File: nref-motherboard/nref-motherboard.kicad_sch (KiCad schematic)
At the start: 219 parts, among them J1 PWR, J10 1-2199230-6, J10 DISP, J11 BAT1, J12 BAT2, J13 SYSCTL_USB, J16 Conn_01x10_Pin, J17 Conn_01x10_Pin, J17 POWSW, J18 Conn_01x20, J19 SER, J2 Conn_01x12_Pin, J5 SYSCTL, J6 USB_INT1, J8 Conn_01x12_Pin, J9 Conn_01x14_Pin, Q1 NTMFD6H840NL, Q2 NTMFD6H840NL, SW2 RESET, SW4 SW_DIP_x08, U1 reform2-som-connector, U10 BQ25756RRVR, U10 W25Q32JVSS, U11 LM62460, U2 MAX1837EUT33+T, U26 74HC573, U4 Si52111-B5, U5 LM62460, U6 PCF8523T, U7 USB2514B_Bi, U8 RP2040, Y2 12MHz 18pF, Y2 24MHz, Y3 25MHz, Y4 32.768 kHz

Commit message: motherboard: specify all parts, complete BOM
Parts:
- C11, C62: Manufacturer_No CL10B103KB8NNNC -> CL05B104KO5NNNC
- C11, C14, C16, C57, C6, C67, C68, C69, C70, C71: Manufacturer_No GRM188R60J476ME15D -> GRM187R61A226ME15D
- C13, C15, C17, C64, C65, C72, C73, C9: MPN CC0402KRX7R7BB104 -> (none); Manufacturer Yageo -> Samsung; Manufacturer_No (none) -> CL05B104KO5NNNC
- C40, C41, C46, C47: Manufacturer (none) -> Taiyo Yuden; Manufacturer_No (none) -> TMK325ABJ476MM-P
- C42, C43, C44, C45, C48, C49: value 100nF -> 0.1uF; Manufacturer (none) -> Samsung; Manufacturer_No (none) -> CL05B104KO5NNNC
- C50: Manufacturer (none) -> Samsung; Manufacturer_No (none) -> CL05Y474KP5VPJC
- C51: Manufacturer (none) -> Samsung; Manufacturer_No (none) -> CL05A104KA5NNNC
- C52, C53: Manufacturer (none) -> Murata; Manufacturer_No (none) -> GRM155C61E475ME15D
- C54, C59, C61, C7: Manufacturer_No CL10B103KB8NNNC -> CL10A474KB8NNNC
- C56, C60: Manufacturer_No CL10B103KB8NNNC -> CL05A104KA5NNNC
- C7, C74, C76, C8: MPN CC0402FRNPO9BN180 -> (none); Manufacturer_No (none) -> CC0402JRNPO9BN180
- C78: Manufacturer Samsung -> Murata; Manufacturer_No CL05B104KO5NNNC -> GRM155C61E475ME15D
- D10, D11, D4: Manufacturer (none) -> Everlight; Manufacturer_No (none) -> 19-217/R6C-AL1M2VY/3T
- D2, D3: Manufacturer (none) -> Taiwan Semi; Manufacturer_No (none) -> TS4148 RCG
- D8, D9: Manufacturer (none) -> Diodes; Manufacturer_No (none) -> SBR1A20T5-7
- H2, H3, H4, H5, H6, H7, R53, TP1, TP2, TP3, TP4: Manufacturer (none) -> DNP; Manufacturer_No (none) -> DNP; now not fitted
- H5: Manufacturer Wurth -> Würth
- J1: Manufacturer HR(Joint Tech Elec) -> JST; Manufacturer_No A2001WR-S-09PD01 -> SM09B-SRSS-TB
- J10, J19: Manufacturer (none) -> JST; Manufacturer_No (none) -> SM06B-SRSS-TB
- J11, J12: Manufacturer (none) -> JST; Manufacturer_No (none) -> SM07B-SRSS-TB
- J13, J5, J6: Manufacturer_No SM04B-SRSS-TB(LF)(SN) -> SM04B-SRSS-TB
- J16, J17: Manufacturer (none) -> Hirose; Manufacturer_No (none) -> FH12-10S-0.5SH(55)
- J17: Manufacturer_No SM02B-SRSS-TB(LF)(SN) -> SM02B-SRSS-TB
- J2, J8: Manufacturer (none) -> Hirose; Manufacturer_No (none) -> FH12-12S-0.5SH(55)
- J9: Manufacturer (none) -> Hirose; Manufacturer_No (none) -> FH12-14S-0.5SH(55)
- L3: LCSC C511026 -> (none); Manufacturer Vishay -> Bourns; Manufacturer_No IHLP4040DZER150M11 -> SRP6030CA-2R2M
- L3: LCSC C511026 -> (none); Manufacturer Vishay -> Pulse; Manufacturer_No IHLP4040DZER150M11 -> PM2205.332NLT
- L5: Manufacturer (none) -> Bourns; Manufacturer_No (none) -> SRP6060FA-100M
- Q1, Q2: Manufacturer (none) -> onsemi; Manufacturer_No (none) -> NVMFD6H840NLWFT1G
- R10: Manufacturer (none) -> Yageo; Manufacturer_No (none) -> RC0402FR-071ML
- R11, R46, R9: Manufacturer Panasonic -> Vishay; Manufacturer_No ERJ2GE0R00X -> CRCW04020000Z0EDC
- R11, R52, R61, R8, R9: Manufacturer (none) -> Yageo; Manufacturer_No (none) -> RC0402FR-0710RL
- R12, R7: Manufacturer (none) -> Ohmite; Manufacturer_No (none) -> LVT12R0050FER
- R15, R26: Manufacturer_No RC0402FR-0710KL -> RC0402FR-07100KL
- R15, R35, R4, R5: MPN CRCW040250K0FKED -> (none); Manufacturer Vishay / Dale -> Yageo; Manufacturer_No (none) -> RC0402FR-0747KL
- R16, R19: Manufacturer_No RC0402FR-07100KL -> RC0402FR-071KL
- R16: Manufacturer_No RC0402FR-073K16L -> RC0402FR-0724K9L
- R18, R31: Manufacturer_No RC0402FR-0710KL -> RC0402FR-074K99L
- R22: MPN RC0402FR-1312KL -> (none); Manufacturer_No (none) -> RC0402FR-0712KL
- R30: Manufacturer_No RC0402FR-073K16L -> RC0402FR-0743K2L
- R34, R69: MPN RC0402FR-071ML -> (none); Manufacturer_No (none) -> RC0402FR-071ML
- R42: MPN CRCW04020000Z0EDC -> (none); Manufacturer Vishay / Dale -> Vishay; Manufacturer_No (none) -> CRCW04020000Z0EDC
- R45, R46, R47, R48, R77, R78: Manufacturer (none) -> Vishay; Manufacturer_No (none) -> CRCW04020000Z0EDC
- R47, R48: Manufacturer UNI-ROYAL -> Yageo; Manufacturer_No 0402WGF274JTCE -> RC0402FR-0727R4L
- R54: Manufacturer (none) -> Yageo; Manufacturer_No (none) -> RC0402FR-0727K4L
- R55: Manufacturer (none) -> Yageo; Manufacturer_No (none) -> RC0402FR-07133KL
- R56: Manufacturer (none) -> Yageo; Manufacturer_No (none) -> RC0402FR-07249KL
- R57: Manufacturer (none) -> Yageo; Manufacturer_No (none) -> RC0402FR-0729K4L
- R58, R59, R74, TH1: Manufacturer (none) -> Yageo; Manufacturer_No (none) -> RC0402FR-0710KL
- R60: value 30.31k -> 30.1k; Manufacturer (none) -> Yageo; Manufacturer_No (none) -> RC0402FR-0730K1L
- R62, R63: Manufacturer (none) -> Yageo; Manufacturer_No (none) -> RC0603JR-070RL
- R65: Manufacturer (none) -> Yageo; Manufacturer_No (none) -> RC0402FR-0720KL
- R70: value 5.24k -> 5.23k; Manufacturer (none) -> Yageo; Manufacturer_No (none) -> AC0402FR-075K23L
- SW2: Manufacturer XKB -> C&K; Manufacturer_No TS-1185EC-C-D-B -> KMR2
- SW4: Manufacturer (none) -> CTS; Manufacturer_No (none) -> 218-8LPSTJ
- U10: Availability In Stock -> (none); Check_prices https://www.snapeda.com/parts/BQ25756RRVR/Texas+Instruments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 -> (none); MANUFACTURER Texas Instruments -> (none); MAXIMUM_PACKAGE_HEIGHT 1.00mm -> (none); MF Texas Instruments -> (none); MP BQ25756RRVR -> (none); Manufacturer (none) -> Texas Instruments; Manufacturer_No (none) -> BQ25756RRVR; PARTREV August 2023 -> (none); Package VFQFN-36 Texas Instruments -> (none); Price None -> (none); Purchase-URL https://www.snapeda.com/api/url_track_click_mouser/?unipart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 -> (none); STANDARD Manufacturer Recommendations -> (none); SnapEDA_Link https://www.snapeda.com/parts/BQ25756RRVR/Texas+Instruments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 -> (none)
- U11, U5: Manufacturer (none) -> Texas Instruments; Manufacturer_No (none) -> LM62460QRPHRQ1
- U4: Manufacturer (none) -> Skyworks; Manufacturer_No (none) -> SI52111-B5-GT
- U7: Manufacturer (none) -> Microchip; Manufacturer_No (none) -> USB2514B/M2
- Y2: Manufacturer Seiko Epson -> Kyocera AVX; Manufacturer_No Q22FA23V0041800 -> CX3225GB12000P0HPQCC
- Y2: MPN TSX-3225 24.0000MF10Z-C3 -> (none); Manufacturer Epson Timing -> Abracon; Manufacturer_No (none) -> ABM8G-24.000MHZ-18-D2Y-T
- Y3: Manufacturer (none) -> Abracon; Manufacturer_No (none) -> ABM8G-25.000MHZ-18-D2Y-T
- Y4: Manufacturer Seiko Epson -> Raltron; Manufacturer_No Q13FC1350000200 -> RT3215-32.768-12.5-TR
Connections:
- no-connect marks 109 -> 115
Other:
- note added: "TODO: 10A with LM61495-Q1"
- note added: "TODO: actually 29.4k, 29.8k doesn't really exist"
- note added: "TODO: electrolytic"

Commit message: motherboard: add bringup notes to schematic
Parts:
- C4, C66: Manufacturer_No CL10B103KB8NNNC -> GRM1555C1H100FA01D
- SW2: Manufacturer_No KMR2 -> KMR223GLFG
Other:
- note added: "TODO: expensive"
- note added: "TODO: look into decoupling VCC and BATteries"
- note added: "TODO: quatsch @ CE"
- note added: "TODO: these 1uFs have the wrong part numbers"
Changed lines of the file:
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@@
 	)
 	(junction
+		(at 403.86 386.08)
+		(diameter 0)
+		(color 0 0 0 0)
+	)
+	(junction
 		(at 328.93 502.92)
 		(diameter 0)
@@
 		)
 	)
+	(text "TODO: these 1uFs have the wrong part numbers"
+		(exclude_from_sim no)
+		(at 345.44 485.14 0)
+		(effects
+			(font
+				(size 1.27 1.27)
+			)
+		)
+	)
 	(text "Rfbt"
 		(exclude_from_sim no)
@@
 		)
 	)
+	(text "TODO: look into decoupling VCC and BATteries"
+		(exclude_from_sim no)
+		(at 547.37 359.41 0)
+		(effects
+			(font
+				(size 1.27 1.27)
+			)
+		)
+	)
 	(text "TODO: connect to rp2040?"
 		(exclude_from_sim no)
@@
 		)
 	)
+	(text "TODO: quatsch @ CE"
+		(exclude_from_sim no)
+		(at 482.6 497.84 0)
+		(effects
+			(font
+				(size 1.27 1.27)
+			)
+		)
+	)
 	(text "MAX 36V"
 		(exclude_from_sim no)
@@
 		)
 	)
+	(text "TODO: expensive"
+		(exclude_from_sim no)
+		(at 467.36 83.82 0)
+		(effects
+			(font
+				(size 1.27 1.27)
+			)
+		)
+	)
 	(text "G"
 		(exclude_from_sim no)
@@
 			)
 		)
-		(property "Manufacturer_No" "CL10B103KB8NNNC"
+		(property "Manufacturer_No" "GRM1555C1H100FA01D"
 			(at 562.61 165.1 0)
 			(effects
@@
 			)
 		)
-		(property "Manufacturer_No" "KMR2"
+		(property "Manufacturer_No" "KMR223GLFG"
 			(at 792.48 130.81 0)
 			(effects
@@
 			)
 		)
-		(property "Manufacturer_No" "CL10B103KB8NNNC"
+		(property "Manufacturer_No" "GRM1555C1H100FA01D"
 			(at 562.61 231.14 0)
 			(effects
@@
 					(unit 1)
 				)
+			)
+		)
+	)
+	(symbol
+		(lib_name "PWR_FLAG_1")
+		(lib_id "power:PWR_FLAG")
+		(at 403.86 386.08 0)
+		(unit 1)
+		(exclude_from_sim no)
+		(in_bom yes)
+		(on_board yes)
+		(dnp no)
+		(fields_autoplaced yes)
+		(property "Reference" "#FLG01"
+			(at 403.86 384.175 0)
+			(effects
+				(font
+					(size 1.27 1.27)
+				)
+				(hide yes)
+			)
+		)
+		(property "Value" "PWR_FLAG"
+			(at 403.86 381 0)
+			(effects
+				(font
+					(size 1.27 1.27)
+				)
+			)
+		)
+		(property "Footprint" ""
+			(at 403.86 386.08 0)
+			(effects
+				(font
+					(size 1.27 1.27)
+				)
+				(hide yes)
+			)
+		)
+		(property "Datasheet" "~"
+			(at 403.86 386.08 0)
+			(effects
+				(font
+					(size 1.27 1.27)
+				)
+				(hide yes)
+			)
+		)
+		(property "Description" "Special symbol for telling ERC where power comes from"
+			(at 403.86 386.08 0)
+			(effects
+				(font
+					(size 1.27 1.27)
+				)
+				(hide yes)
+			)
+		)
+		(pin "1"
+		)
+		(instances
+			(project ""
+				(path "/a432b2af-5748-42a5-94fe-8be4ed1e5510"
+					(reference "#FLG01")
+					(unit 1)
+				)

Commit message: WIP mobo d2 snapshot
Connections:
- net +3V3: now also J16.10 (Pin_10), J17.10 (Pin_10); no longer J16.1 (Pin_1), J17.1 (Pin_1)
- net +5V: now also J2.10 (Pin_10), J2.11 (Pin_11), J8.10 (Pin_10), J8.11 (Pin_11); no longer J2.2 (Pin_2), J2.3 (Pin_3), J8.2 (Pin_2), J8.3 (Pin_3)
- net DAC_BCLK: now also J17.3 (Pin_3); no longer J17.8 (Pin_8)
- net DAC_DIN: now also J17.6 (Pin_6); no longer J17.5 (Pin_5)
- net DAC_DOUT: now also J17.7 (Pin_7); no longer J17.4 (Pin_4)
- net DAC_MCLK: now also J17.2 (Pin_2); no longer J17.9 (Pin_9)
- net DAC_SCL: now also J17.8 (Pin_8); no longer J17.3 (Pin_3)
- net DAC_SDA: now also J17.9 (Pin_9); no longer J17.2 (Pin_2)
- net DAC_TXFS: now also J17.5 (Pin_5); no longer J17.6 (Pin_6)
- net ETH0_A+: now also J9.11 (Pin_11); no longer J9.4 (Pin_4)
- net ETH0_A-: now also J9.10 (Pin_10); no longer J9.5 (Pin_5)
- net ETH0_B+: now also J9.8 (Pin_8); no longer J9.7 (Pin_7)
- net ETH0_B-: now also J9.7 (Pin_7); no longer J9.8 (Pin_8)
- net ETH0_C+: now also J9.5 (Pin_5); no longer J9.10 (Pin_10)
- net ETH0_C-: now also J9.4 (Pin_4); no longer J9.11 (Pin_11)
- net ETH0_D+: now also J9.2 (Pin_2); no longer J9.13 (Pin_13)
- net ETH0_D-: now also J9.1 (Pin_1); no longer J9.14 (Pin_14)
- net ETH0_LED_LINK1: now also J9.14 (Pin_14); no longer J9.1 (Pin_1)
- net ETH0_LED_RX: now also J9.13 (Pin_13); no longer J9.2 (Pin_2)
- net GND: now also J16.1 (Pin_1), J16.7 (Pin_7), J17.1 (Pin_1), J17.4 (Pin_4), J2.12 (Pin_12), J2.3 (Pin_3), J2.6 (Pin_6), J2.9 (Pin_9), J8.12 (Pin_12), J8.3 (Pin_3), J8.6 (Pin_6), J8.9 (Pin_9); no longer J16.10 (Pin_10), J16.4 (Pin_4), J17.10 (Pin_10), J17.7 (Pin_7), J2.1 (Pin_1), J2.10 (Pin_10), J2.4 (Pin_4), J2.7 (Pin_7), J8.1 (Pin_1), J8.10 (Pin_10), J8.4 (Pin_4), J8.7 (Pin_7)
- net SD_CLK: now also J16.8 (Pin_8); no longer J16.3 (Pin_3)
- net SD_CMD: now also J16.6 (Pin_6); no longer J16.5 (Pin_5)
- net SD_D0: now also J16.2 (Pin_2); no longer J16.9 (Pin_9)
- net SD_D1: now also J16.3 (Pin_3); no longer J16.8 (Pin_8)
- net SD_D2: now also J16.4 (Pin_4); no longer J16.7 (Pin_7)
- net SD_D3: now also J16.5 (Pin_5); no longer J16.6 (Pin_6)
- net SD_DET: now also J16.9 (Pin_9); no longer J16.2 (Pin_2)
- net USB1_DN: now also J8.1 (Pin_1); no longer J8.12 (Pin_12)
- net USB1_DP: now also J8.2 (Pin_2); no longer J8.11 (Pin_11)
- net USB1_RXN: now also J8.7 (Pin_7); no longer J8.6 (Pin_6)
- net USB1_RXP: now also J8.8 (Pin_8); no longer J8.5 (Pin_5)
- net USB1_TXN: now also J8.4 (Pin_4); no longer J8.9 (Pin_9)
- net USB1_TXP: now also J8.5 (Pin_5); no longer J8.8 (Pin_8)
- net USB2A_DN: now also J2.1 (Pin_1); no longer J2.12 (Pin_12)
- net USB2A_DP: now also J2.2 (Pin_2); no longer J2.11 (Pin_11)
- net USB2_RXN: now also J2.7 (Pin_7); no longer J2.6 (Pin_6)
- net USB2_RXP: now also J2.8 (Pin_8); no longer J2.5 (Pin_5)
- net USB2_TXN: now also J2.4 (Pin_4); no longer J2.9 (Pin_9)
- net USB2_TXP: now also J2.5 (Pin_5); no longer J2.8 (Pin_8)
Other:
- note added: "1GBe to port farm (flipped in D-2!)"
- note added: "I2S Audio (flipped in D-2!)"
- note added: "SD Card (flipped in D-2)!)"
- note added: "TODO: DNP on these 49.9... except if we use clock gen"
- note added: "TODO: diodes here inducing VPP so we can run without charging/batteries"
- note added: "TODO: replaced with 20k resistor on board, 10k = 25 degrees. clears TS fault"
- note added: "TODO: why not use 2x clock gen?"
- note added: "USB3 to port farm 1 (flipped in D-2!)"
- note added: "USB3 to port farm 2 (flipped in D-2!)"
- note added: "currently 4.7k fitted"
- note added: "removed on board and connected to GND"
- note added: "replaced with 0R on MB"
- note removed: "1GBe to port farm"
- note removed: "I2S Audio"
- note removed: "SD Card"
- note removed: "USB3 to port farm 1"
- note removed: "USB3 to port farm 2"

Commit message: motherboard: d-2 routing snapshot (0 unrouted)
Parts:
- removed TH1: 10k, Resistor_SMD:R_0402_1005Metric, symbol Device:Thermistor_NTC
- removed TP4: TestPoint, TestPoint:TestPoint_Pad_1.0x1.0mm, symbol Connector:TestPoint
- added C80: 0.1uF, Capacitor_SMD:C_0402_1005Metric, symbol Device:C_Small
- added D12, D13: SBR1A30T5-7, Diode_SMD:D_SOD-523, symbol Device:D_Schottky_Small
- added R66, R67, R80, R81: 10k, Resistor_SMD:R_0402_1005Metric, symbol Device:R_Small
- added R79: 0, Resistor_SMD:R_0402_1005Metric, symbol Device:R_Small
- added U12: TS3USB30EDGSR, Package_SO:VSSOP-10_3x3mm_P0.5mm, symbol Interface_USB:TS3USB30EDGSR
- D8, D9: value SBR1A20T5-7 -> SBR1A30T5-7; Manufacturer_No SBR1A20T5-7 -> SBR1A30T5-7
- H2, H3, H4, H5: footprint MountingHole:MountingHole_2.2mm_M2_Pad -> MountingHole:MountingHole_2.5mm_Pad
- R58, R59: value 10k -> 0
- R74: value 10k -> DNP
- R77, R78: value 0 -> 4.7k
- SW2: value RESET -> SYS_RESET
- TP3: footprint TestPoint:TestPoint_Pad_1.0x1.0mm -> TestPoint:TestPoint_Pad_D1.0mm; Manufacturer DNP -> (none); Manufacturer_No DNP -> (none); now fitted
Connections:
- net GND: now also C80.2, R66.1, R67.2, R80.2, R81.2, U12.5 (GND)
- net HDMI_AUXN: now also U12.7 (D2-)
- net HDMI_AUXP: now also U12.3 (D2+); no longer TP3.1
- net HDMI_SCL: now also U12.8 (D1-); no longer J18.16 (Pin_16)
- net HDMI_SDA: now also U12.2 (D1+); no longer J18.15 (Pin_15)
- net IMX_RESETn: now also TP3.1
- net STANDBY_3V3: now also R79.1
- net VCC: now also D13.2 (A); no longer C2.1, R72.1, U2.3 (IN)
- net VPD: now also D12.2 (A)
- net ~{CHRG_CE}: now also R66.2
- net at R60.2, R70.1, U10.8 (TS): now also R81.1
- net RP_FUSB_INT: no longer names the net of U8.17 (GPIO14)
- net USB_SRC_EN renamed HDMI_DP_SWITCH
- net HDMI_DP_SWITCH: now also R80.1, U12.1 (S)
- new net: C80.1, R79.2, U12.10 (VCC)
- new net: R67.1, U12.9 (~{OE})
- new net: C2.1, D12.1 (K), D13.1 (K), R72.1, U2.3 (IN)
- new net HDMI_SCL_AUXN: J18.16 (Pin_16), U12.6 (D-)
- new net HDMI_SDA_AUXP: J18.15 (Pin_15), U12.4 (D+)
- no-connect marks 115 -> 114
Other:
- note added: "0: D=D1 (HDMI DDC) 1: D=D2 (DP AUX)"
- note added: "Diode ORing battery and PD power to standby supply"
- note added: "HDMI/DP to port farm"
- note added: "TODO: look into decoupling VCC and BATteries perhaps switch to BQ25750"
- note added: "TODO: this was a TH replaced with 20k resistor on board, 10k = 25 degrees. clears TS fault"
- note added: "new in D-2: HDMI DDC vs DP AUX mux"
- note removed: "HDMI to port farm"
- note removed: "TODO: AUX for DP?"
- note removed: "TODO: buffer I2C?"
- note removed: "TODO: connect to rp2040?"
- note removed: "TODO: diodes here inducing VPP so we can run without charging/batteries"
- note removed: "TODO: look into decoupling VCC and BATteries"
- note removed: "TODO: quatsch @ CE"
- note removed: "TODO: replaced with 20k resistor on board, 10k = 25 degrees. clears TS fault"
- note removed: "TODO: unaccounted for!"
- note removed: "lets do them as I2C GPIO on power input board"
- note removed: "replaced with 0R on MB"
- moved on the sheet: J18, R21, R30, R56, SW2

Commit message: motherboard d-2 routing complete
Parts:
- removed TP1, TP2: TestPoint, TestPoint:TestPoint_Pad_1.0x1.0mm, symbol Connector:TestPoint
- added C81, C82, C83, C84, C85, C86, C87, C97: 10uF, Capacitor_SMD:C_0603_1608Metric, symbol Device:C_Small
- added C88, C89, C90, C91, C93, C94: 4.7uF, Capacitor_SMD:C_0603_1608Metric, symbol Device:C_Small
- added C92: 47uF, Capacitor_SMD:C_0603_1608Metric, symbol Device:C_Small
- added C95, C96: 0.1uF, Capacitor_SMD:C_0402_1005Metric, symbol Device:C_Small
- added FB3: 100@100MHz 3A, Inductor_SMD:L_0603_1608Metric, symbol pocket-reform-motherboard-rescue:Ferrite_Bead_Small-Device
- added FB4: 220@100MHz 1.4A, Inductor_SMD:L_0603_1608Metric, symbol Device:FerriteBead_Small
- added J14: USB_INT2, Connector_JST:JST_SH_SM04B-SRSS-TB_1x04-1MP_P1.00mm_Horizontal, symbol Connector:Conn_01x04_Male
- added J3: 10102166A812A, footprints:10102166A812A, symbol 10102166A812A:10102166A812A
- added R82: 0, Resistor_SMD:R_0402_1005Metric, symbol Device:R_Small
- added R83, R84: 49.9, Resistor_SMD:R_0402_1005Metric, symbol Device:R_Small
- added U13: TLV75712PDBV, Package_TO_SOT_SMD:SOT-23-5, symbol Regulator_Linear:TLV75712PDBV
- added U14: TLV75718PDBV, Package_TO_SOT_SMD:SOT-23-5, symbol Regulator_Linear:TLV75718PDBV
- H5: value NGFF-Mount1 -> NGFF-Mount
- H6: footprint footprints:nref-reflex-logo -> footprints:nref-logo
- U4: value Si52111-B5 -> Si52112-B5; symbol Si52111-B5:Si52111-B5 -> Si52111-B5:Si52112-B5; Manufacturer_No SI52111-B5-GT -> SI52112-B5-GT
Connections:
- net +3V3: now also C81.1, C82.1, C85.1, C88.1, C94.1, FB3.1, U13.1 (IN), U13.3 (EN), U14.1 (IN), U14.3 (EN)
- net +5V: now also C83.1, C84.1, C86.1, C87.1, FB4.1
- net GND: now also C81.2, C82.2, C83.2, C84.2, C85.2, C86.2, C87.2, C88.2, C89.2, C90.2, C91.2, C92.2, C93.2, C94.2, C97.2, J14.4 (Pin_4), J3.10, J3.13, J3.16, J3.6, J3.S1, J3.S2, J3.S3, J3.S4, J3.S5, J3.S6, R83.1, R84.1, U13.2 (GND), U14.2 (GND)
- net PCIE1_CLK_N: now also J3.8, R83.2
- net PCIE1_CLK_P: now also J3.7, R84.2
- net PCIE1_RESETn: now also R82.1
- net PCIE1_RX_N: now also C95.2
- net PCIE1_RX_P: now also C96.2
- net PCIE1_TX_N: now also J3.12
- net PCIE1_TX_P: now also J3.11
- net PCIE2_CLK2_N: now also U4.8 (DIFF2_N); no longer U1.67 (CSI_P2_CK_N)
- net PCIE2_CLK2_P: now also U4.7 (DIFF2_P); no longer U1.69 (CSI_P2_CK_P)
- net USB2D_DN: now also J14.2 (Pin_2)
- net USB2D_DP: now also J14.3 (Pin_3)
- new net: C92.1, FB3.2, J3.4
- new net: J3.2, R82.2
- new net: C97.1, FB4.2, J14.1 (Pin_1)
- new net +1V2: C90.1, C93.1, J3.17, U13.5 (OUT)
- new net +1V8: C89.1, C91.1, J3.9, U14.5 (OUT)
- new net PCIE1_RX_CAP_N: C95.1, J3.14
- new net PCIE1_RX_CAP_P: C96.1, J3.15
- no-connect marks 114 -> 120
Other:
- note added: "1V8 supply for MicroSD Express"
- note added: "D-2: exchanged to 2x clock gen"
- note added: "M Key M.2"
- note added: "MicroSD Express Connector Amphenol 10102166A812A"
- note added: "TODO: might need 220nF"
- note removed: "TODO: DNP on these 49.9... except if we use clock gen"
- note removed: "TODO: why not use 2x clock gen?"
- note removed: "buffered clock from module coming back"
- moved on the sheet: C39, C79, FB1, H5, J10, J13, J5, J6, U6, Y4

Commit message: add latest PCB updates
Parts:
- C88, C89, C90, C91, C93, C94: Manufacturer (none) -> Murata; Manufacturer_No (none) -> GCJ188C70J475KE02D
- C95, C96: Manufacturer (none) -> Samsung; Manufacturer_No (none) -> CL05B104KO5NNNC
- D10, D11, D23, D4: Manufacturer Everlight -> Vishay; Manufacturer_No 19-217/R6C-AL1M2VY/3T -> VLMS1300-GS08
- J3: Manufacturer (none) -> Amphenol; Manufacturer_No (none) -> 10102166A812A
- L1: Manufacturer YJYCOIN -> Taiyo Yuden; Manufacturer_No YNR3015-150M -> NRH3012T220MN
- R58, R59: Manufacturer Yageo -> Vishay; Manufacturer_No RC0402FR-0710KL -> CRCW04020000Z0EDC
- R67, R80: Manufacturer Vishay -> Yageo; Manufacturer_No CRCW04020000Z0EDC -> RC0402FR-0710KL
- R77, R78: Manufacturer Vishay -> Yageo; Manufacturer_No CRCW04020000Z0EDC -> RC0402FR-074K7L
- TP3: Manufacturer (none) -> DNP; Manufacturer_No (none) -> DNP; now not fitted
- U12: Manufacturer (none) -> Texas Instruments; Manufacturer_No (none) -> TS3USB30EDGSR
- U13: Manufacturer (none) -> Texas Instruments; Manufacturer_No (none) -> TLV75712PDBVR
- U14: Manufacturer (none) -> Texas Instruments; Manufacturer_No (none) -> TLV75718PDBVR
- U8: Manufacturer_No RP2040 -> SC0914
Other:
- note added: "TODO: change to standard 0606"
- note added: "mouser alt: broadcom HSMF-C125"

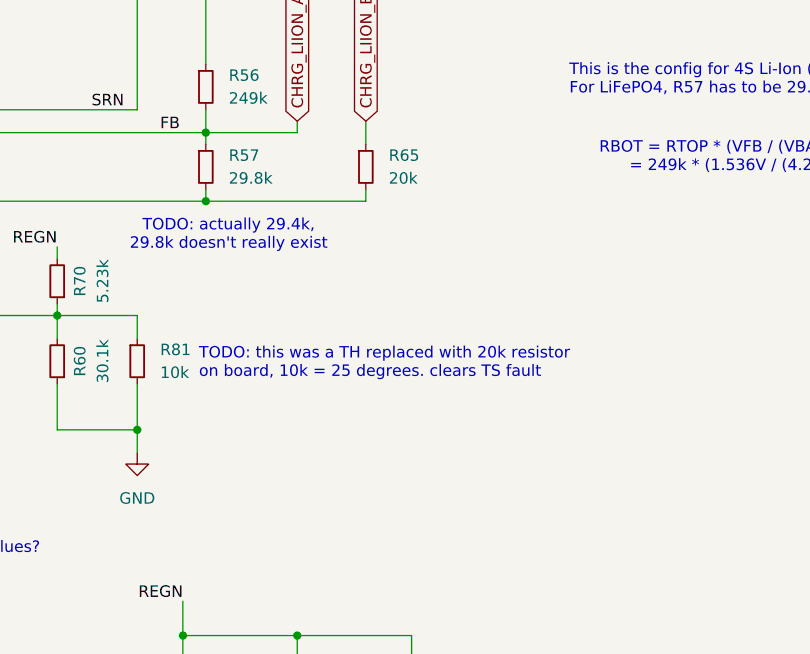
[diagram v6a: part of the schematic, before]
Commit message: motherboard: add some notes
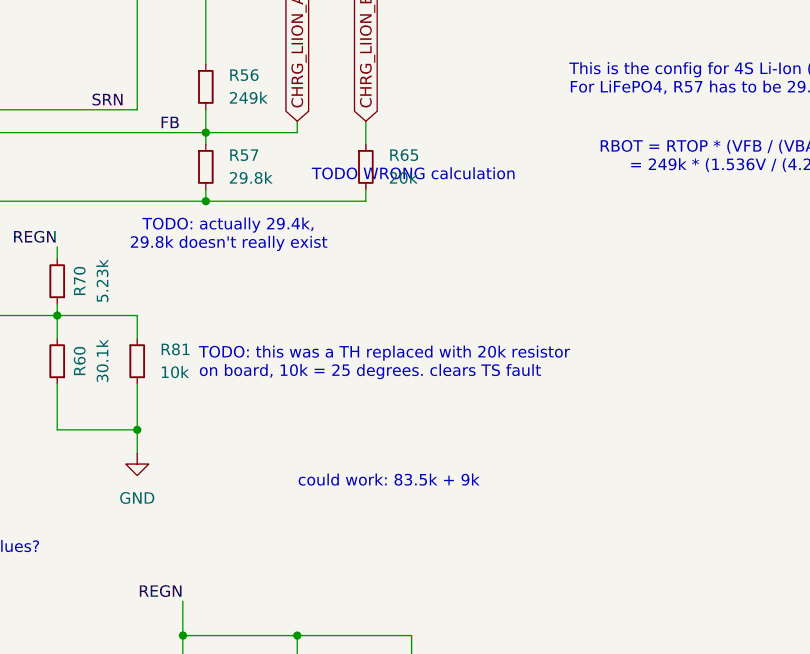
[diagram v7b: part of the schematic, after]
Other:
- note added: "TODO WRONG calculation"
- note added: "could work: 83.5k + 9k"
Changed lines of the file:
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@@
+		)
+	)
+	(text "could work: 83.5k + 9k"
+		(exclude_from_sim no)
+		(at 551.18 512.572 0)
+		(effects
+			(font
+				(size 1.27 1.27)
+			)
 		)
 	)
@@
 		(effects
 			(font
+				(size 1.27 1.27)
+			)
+		)
+	)
+	(text "TODO WRONG calculation"
+		(exclude_from_sim no)
+		(at 553.974 478.536 0)
+		(effects
+			(font
